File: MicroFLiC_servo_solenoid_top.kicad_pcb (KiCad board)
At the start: 2 copper layers, 49.8 x 49.8 mm, 37 parts, among them P1 1x14 header strip, P10 1x4 socket strip, P11 2x3 header strip R/A, P12 2x3 header strip R/A, P2 1x14 socket strip, P3 12-way Micro-MaTch, P4 Jack_3.5mm_3pin, P5 Jack_3.5mm_3pin, P6 RCA_3, P7 RCA_3, P8 1x6 socket strip, P9 1x4 header strip, U1 PCA9306DP, U2 DRV103, U3 DRV103, U4 MCP4728

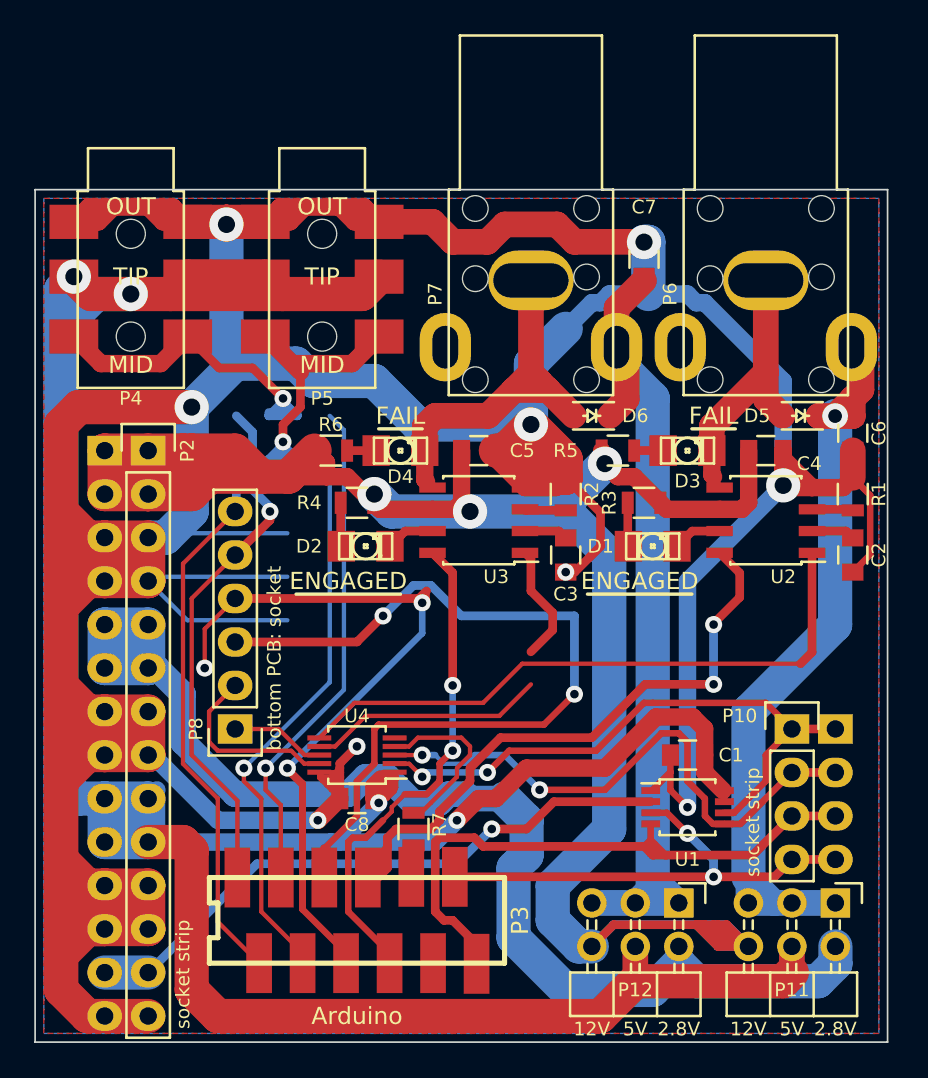
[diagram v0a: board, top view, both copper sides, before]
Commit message: Created v1.1, got rid of all redundant parts for separate top and bottom boards
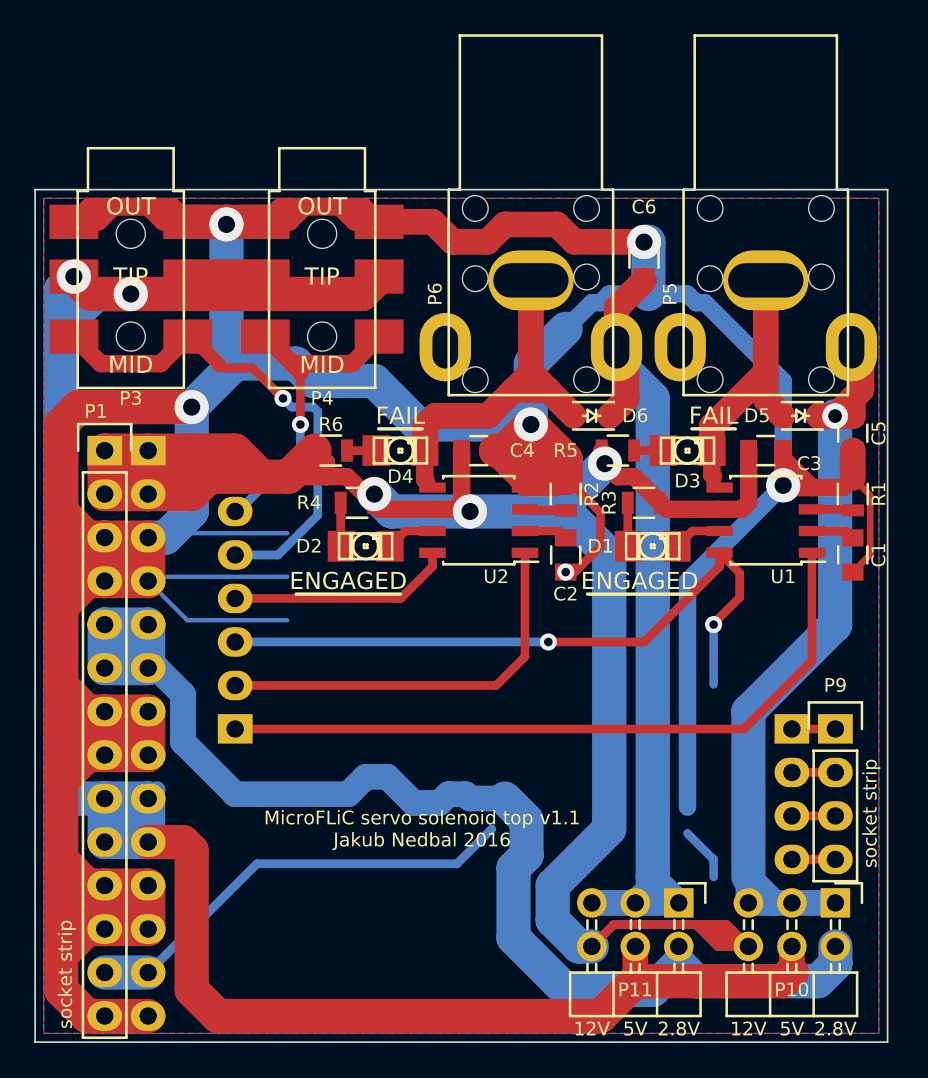
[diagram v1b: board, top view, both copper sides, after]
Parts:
- removed the C1 at (138.2, 133.1)
- removed C8: 100n, Capacitors_SMD:C_0805
- removed the P10 at (144.3, 131.6)
- removed the P3 at (118.9, 142.7)
- removed R7: 0R, Resistors_SMD:R_0805
- removed the U1 at (138.2, 136.1)
- removed U4: MCP4728, Housings_SSOP:MSOP-10_3x3mm_Pitch0.5mm
- added P7: 1x6 header strip, Pin_Headers:Pin_Header_Straight_1x06, B.Cu at (111.8, 131.6)
- P1: value 1x14 header strip -> 1x14 socket strip; footprint Pin_Headers:Pin_Header_Straight_1x14 -> jakub:ESQ-114-33-G-S; moved to F.Cu
- P2: value 1x14 socket strip -> 1x14 header strip; footprint jakub:ESQ-114-33-G-S -> Pin_Headers:Pin_Header_Straight_1x14; moved to B.Cu
- P8: value 1x6 socket strip -> 1x4 header strip; footprint jakub:ESQ-106-33-G-S -> Pin_Headers:Pin_Header_Straight_1x04; moved to B.Cu
- P9: value 1x4 header strip -> 1x4 socket strip; footprint Pin_Headers:Pin_Header_Straight_1x04 -> jakub:ESQ-104-33-G-S; moved to F.Cu
- moved P8 32.5 mm to (144.3, 131.6), turned to 180 degrees
- turned P1 to 0 degrees
- turned P2 to 180 degrees
- turned P9 to 270 degrees
- renumbered C2 to C1, C3 to C2, C4 to C3, C5 to C4, C6 to C5, C7 to C6, P11 to P10, P12 to P11, P4 to P3, P5 to P4, P6 to P5, P7 to P6, U2 to U1, U3 to U2
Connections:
- net /shutterPWM/DA renamed /shutterPWM/DC
- net /shutterPWM/DB renamed /shutterPWM/DD
- net /shutterPWM/EA renamed /shutterPWM/EC
- net /shutterPWM/EB renamed /shutterPWM/ED
- net /shutterPWM/ENG_A renamed /shutterPWM/ENG_C
- net /shutterPWM/ENG_B renamed /shutterPWM/ENG_D
- net /shutterPWM/FA renamed /shutterPWM/FC
- net /shutterPWM/FB renamed /shutterPWM/FD
- net /shutterPWM/OA renamed /shutterPWM/OC
- net /shutterPWM/OB renamed /shutterPWM/OD
- net /shutterPWM/SHA_O/C renamed /shutterPWM/SHC_O/C
- net /shutterPWM/SHA_PWR renamed /shutterPWM/SHC_PWR
- net /shutterPWM/SHB_O/C renamed /shutterPWM/SHD_O/C
- net /shutterPWM/SHB_PWR renamed /shutterPWM/SHD_PWR
- P3 pad 2: /SERVO1 -> /SERVO3
- P4 pad 2: /SERVO2 -> /SERVO4
- P8 pad 1: /shutterPWM/SH3_PWM -> /SCL_5V
- P8 pad 2: /shutterPWM/SH4_PWM -> /SDA_5V
- P8 pad 3: /SH3 -> /SDA_3V3
- P8 pad 4: /SH4 -> /SCL_3V3
- P9 pad 1: /I2C/SCL_5V -> /SCL_5V
- P9 pad 2: /I2C/SDA_5V -> /SDA_5V
- P9 pad 3: /I2C/SDA_3V3 -> /SDA_3V3
- P9 pad 4: /I2C/SCL_3V3 -> /SCL_3V3
- U1 pad 1: /shutterPWM/SH1_PWM -> /shutterPWM/SH3_PWM
- U1 pad 8: /shutterPWM/SH1 -> /shutterPWM/SH3
- U2 pad 1: /shutterPWM/SH2_PWM -> /shutterPWM/SH4_PWM
- U2 pad 8: /shutterPWM/SH2 -> /shutterPWM/SH4
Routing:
- net +5VP: track 186.7 -> 129.3 mm, vias 4 -> 2
- net /SERVO2: track 51.7 -> 0.00 mm, vias 2 -> 0
- net /SH4: track 51.5 -> 0.00 mm, vias 3 -> 0
- net /SERVO1: track 50.6 -> 0.00 mm, vias 2 -> 0
- net /SH3: track 50.6 -> 0.00 mm, vias 2 -> 0
- net /shutterPWM/SH1: track 40.4 -> 0.00 mm, vias 2 -> 0
- net /shutterPWM/SH3: track 0.00 -> 39.7 mm, vias 0 -> 2
- net /I2C/SDA_3V3: track 37.8 -> 0.00 mm
- net /shutterPWM/SH1_PWM: track 36.8 -> 0.00 mm
- net /shutterPWM/SH3_PWM: track 5.54 -> 41.6 mm
- net /I2C/SCL_5V: track 35.7 -> 0.00 mm, vias 2 -> 0
- net /I2C/SDA_5V: track 33.7 -> 0.00 mm, vias 2 -> 0
- net /shutterPWM/SH2: track 31.9 -> 0.00 mm, vias 2 -> 0
- net GND: track 356.6 -> 327.0 mm, vias 9 -> 6
- net /I2C/SCL_3V3: track 28.5 -> 0.00 mm, vias 2 -> 0
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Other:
- board text added: "MicroFLiC servo solenoid top v1.1 Jakub Nedbal 2016"
- board text removed: "Arduino"
- board text removed: "bottom PCB: socket"
- board text removed: "top PCB: pin header"

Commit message: Added better de-bouncing diode description
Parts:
- P3, P4: value Jack_3.5mm_3pin -> 3.5mm jack
- P5, P6: value RCA_3 -> RCA jack
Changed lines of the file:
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@@
   (page A4)
   (layers
-    (0 F.Cu signal hide)
-    (31 B.Cu signal hide)
+    (0 F.Cu signal)
+    (31 B.Cu signal)
     (32 B.Adhes user)
     (33 F.Adhes user)
@@
       (effects (font (size 0.8 0.8) (thickness 0.12)))
     )
-    (fp_text value RCA_3 (at -1.016 0 360) (layer F.SilkS) hide
+    (fp_text value "RCA jack" (at -1.016 0 360) (layer F.SilkS) hide
       (effects (font (size 1 1) (thickness 0.15)))
     )
@@
       (effects (font (size 0.8 0.8) (thickness 0.12)))
     )
-    (fp_text value RCA_3 (at 0 6.35 270) (layer F.SilkS) hide
+    (fp_text value "RCA jack" (at 0 6.35 270) (layer F.SilkS) hide
       (effects (font (size 1 1) (thickness 0.15)))
     )
@@
       (effects (font (size 0.8 0.8) (thickness 0.12)))
     )
-    (fp_text value Jack_3.5mm_3pin (at 9.525 0 360) (layer F.SilkS) hide
+    (fp_text value "3.5mm jack" (at 9.525 0 360) (layer F.SilkS) hide
       (effects (font (size 1 1) (thickness 0.15)))
     )
@@
       (effects (font (size 0.8 0.8) (thickness 0.12)))
     )
-    (fp_text value Jack_3.5mm_3pin (at 9.525 0 360) (layer F.SilkS) hide
-      (effects (font (size 1 1) (thickness 0.15)))
-    )
+    (fp_text value "3.5mm jack" (at 9.525 0 360) (layer F.SilkS) hide
+      (effects (font (size 1 1) (thickness 0.15)))
+    )

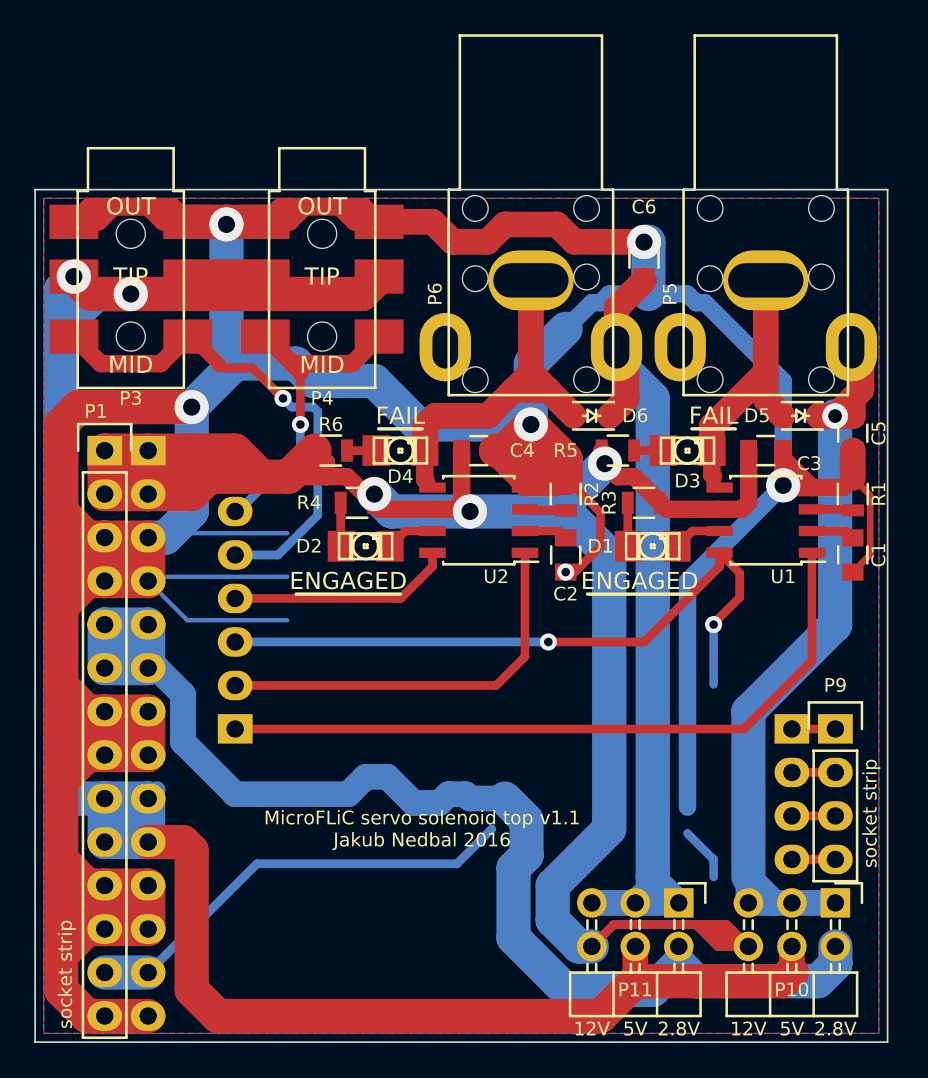
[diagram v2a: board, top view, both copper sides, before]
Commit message: Changed ENGAGED LED anode to +5V, changed SOD-323 packages, tidied up layout
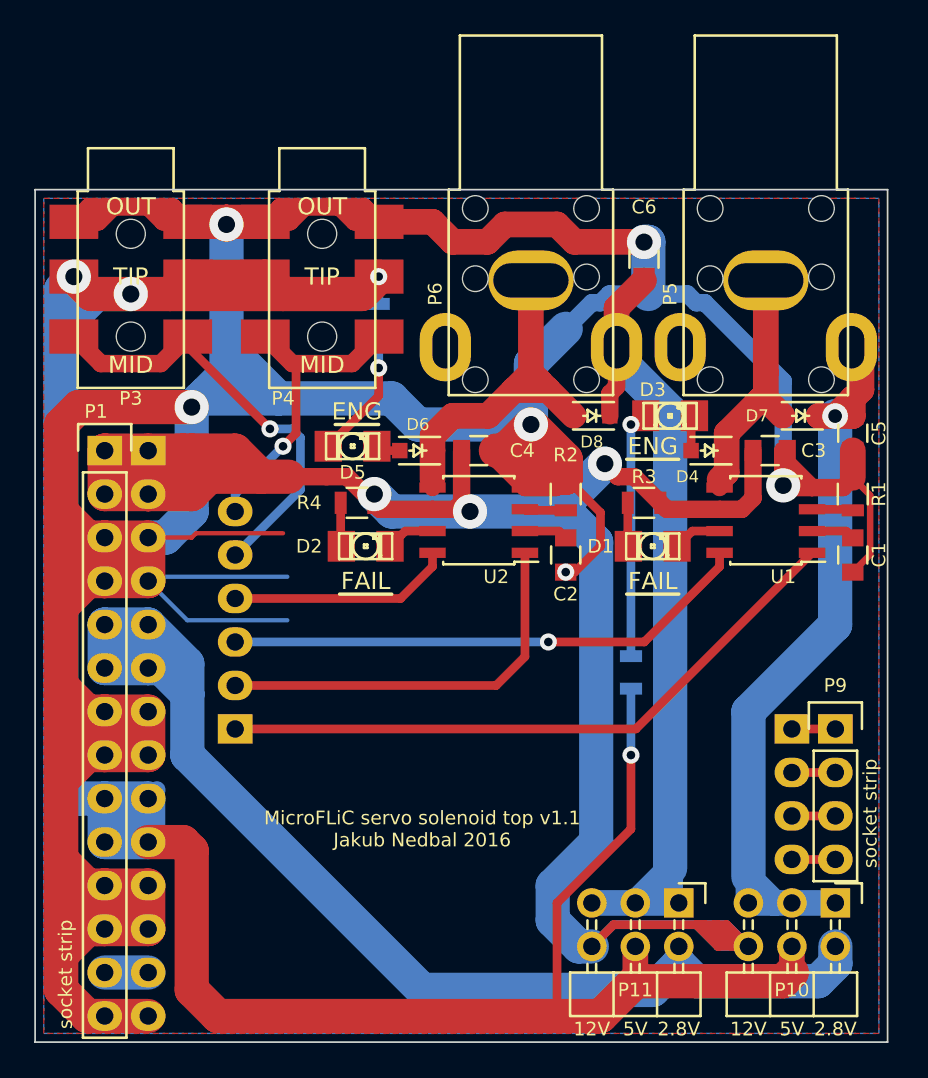
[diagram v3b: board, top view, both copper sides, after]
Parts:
- added D4: 1N4148, jakub:SOD-323, F.Cu at (139.4, 115.3)
- added D6: 1N4148, jakub:SOD-323, F.Cu at (122.4, 115.3)
- D7: renamed from D5; footprint Diodes_SMD:SOD-323 -> jakub:SOD-323
- D8: renamed from D6; footprint Diodes_SMD:SOD-323 -> jakub:SOD-323
- R5, R6: value 10k -> 3k; moved to B.Cu
- moved R5 13.0 mm to (134.9, 128.3), turned to 270 degrees
- moved R6 8.12 mm to (120.1, 107.7), turned to 90 degrees
- moved D5 2.81 mm to (118.6, 115.1)
- moved D3 2.27 mm to (137.2, 113.3)
- moved C3 0.25 mm to (143.0, 115.3)
- renumbered D4 to D5
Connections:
- net /shutterPWM/ENG_C renamed /shutterPWM/FAIL_C
- net /shutterPWM/ENG_D renamed /shutterPWM/FAIL_D
- D1 pad 2: /shutterPWM/EC -> /shutterPWM/FC
- D2 pad 2: /shutterPWM/ED -> /shutterPWM/FD
- D3 pad 1: /shutterPWM/SHC_O/C -> /shutterPWM/EC2
- D3 pad 2: /shutterPWM/FC -> /shutterPWM/EC1
- D5 pad 1: /shutterPWM/SHD_O/C -> /shutterPWM/ED2
- D5 pad 2: /shutterPWM/FD -> /shutterPWM/ED1
- R3 pad 1: /shutterPWM/EC -> /shutterPWM/FC
- R4 pad 1: /shutterPWM/ED -> /shutterPWM/FD
- R5 pad 1: /shutterPWM/FC -> /shutterPWM/EC1
- R5 pad 2: +12V -> +5VP
- R6 pad 1: /shutterPWM/FD -> /shutterPWM/ED1
- R6 pad 2: +12V -> +5VP
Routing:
- net +3V3: track 26.1 -> 2.54 mm
- net +5VP: track 129.3 -> 151.9 mm, vias 2 -> 4
- net GND: track 327.0 -> 311.8 mm
- net /shutterPWM/EC1: track 0.00 -> 14.5 mm, vias 0 -> 1
- net /shutterPWM/SH3: track 39.7 -> 30.9 mm, vias 2 -> 1
- net /shutterPWM/ED1: track 0.00 -> 7.64 mm, vias 0 -> 1
- net /SERVO3: track 32.3 -> 26.2 mm
- net +12V: track 155.2 -> 149.9 mm
- net /shutterPWM/SH3_PWM: track 41.6 -> 37.9 mm
- net (no net): track 3.17 -> 0.00 mm
- net /shutterPWM/ED: track 2.61 -> 0.00 mm
- net /shutterPWM/EC: track 2.56 -> 0.00 mm
- net /shutterPWM/SHD_PWR: track 49.2 -> 51.8 mm
- net /shutterPWM/EC2: track 0.00 -> 2.11 mm
- net /shutterPWM/ED2: track 0.00 -> 1.44 mm
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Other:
- board text added: "ENG"
- board text removed: "ENGAGED"
